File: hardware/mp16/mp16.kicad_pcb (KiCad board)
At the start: 2 copper layers, 76.2 x 104.8 mm, 161 parts, among them J2 OLED SSD1306 I2C, J3 USB-C, J4 MIDI IN, J5 MIDI OUT, J6 EXPANSION, J7 LiPo 1S (pin 1 = GND, pin 2 =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, Q1 DMG2305UX, Q2 MMBT3906, SW1 SHIFT, SW10 P9, SW11 P10, SW12 P11, SW13 P12, SW14 P13, SW15 P14, SW16 P15, SW17 P16, SW18 BOOT, SW19 RESET, SW2 P1, SW20 Power, SW3 P2, SW4 P3, SW5 P4, SW6 P5, SW7 P6, SW8 P7, SW9 P8, U1 74HC165, U10 RP2040, U11 W25Q128JV, U12 USBLC6-2SC6, U13 BQ24074, U15 MAX17048, U16 TPS22917, U17 AP2112K-3.3, U18 MT3608, U19 TLP109, U2 74HC165, U20 USBLC6-2SC6, U3 74HC165, U4 74AHCT1G125, Y1 12MHz

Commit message: BOOT and RESET side by side with labels; fixed-part list; HIDE_REFS
BOOT (SW18) and RESET (SW19) stand side by side in the lower left of the
open bottom shell's window, each named on the bottom silkscreen, the SWD
pads in a row above them (order in hardware/README.md). MIDI In parts
moved to make room. tools/pcb.py: design.HIDE_REFS hides references a
label already names. The side-view charge LED joins the parts that never
move; the battery plug may move (Samuel). Not yet routed.

Co-Authored-By: Claude Opus 5.5 <noreply@anthropic.com>
Claude-Session: https://claude.ai/code/session_01P864NL83Ce2Z2DY4mgeMiF
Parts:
- C55, C56: footprint Capacitor_SMD:C_0402_1005Metric -> Capacitor_SMD:C_0603_1608Metric
- moved SW18 28.5 mm to (68.6, 56.5), turned to -90 degrees
- moved C71 9.28 mm to (57.8, 48.0), turned to -90 degrees
- moved R41 5.69 mm to (57.8, 51.0), turned to -90 degrees
- moved SW19 5.41 mm to (63.4, 56.5), turned to -90 degrees
- moved R11 2.92 mm to (77.5, 53.3)
- moved C54 2.22 mm to (86.4, 59.0)
- moved C56 1.93 mm to (88.5, 59.5), turned to -90 degrees
- moved U19 1.00 mm to (61.0, 49.0)
- moved C55 0.90 mm to (84.4, 59.5), turned to -90 degrees
- moved TP1 0.40 mm to (66.2, 52.6)
- moved TP2 0.40 mm to (68.4, 52.6)
- moved TP3 0.40 mm to (70.6, 52.6)
- moved U16 0.20 mm to (86.6, 56.2)
- moved D22 0.10 mm to (60.8, 43.4)
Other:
- board text added: "BOOT"
- board text added: "PATS MP-16 rev 2"
- board text added: "RESET"

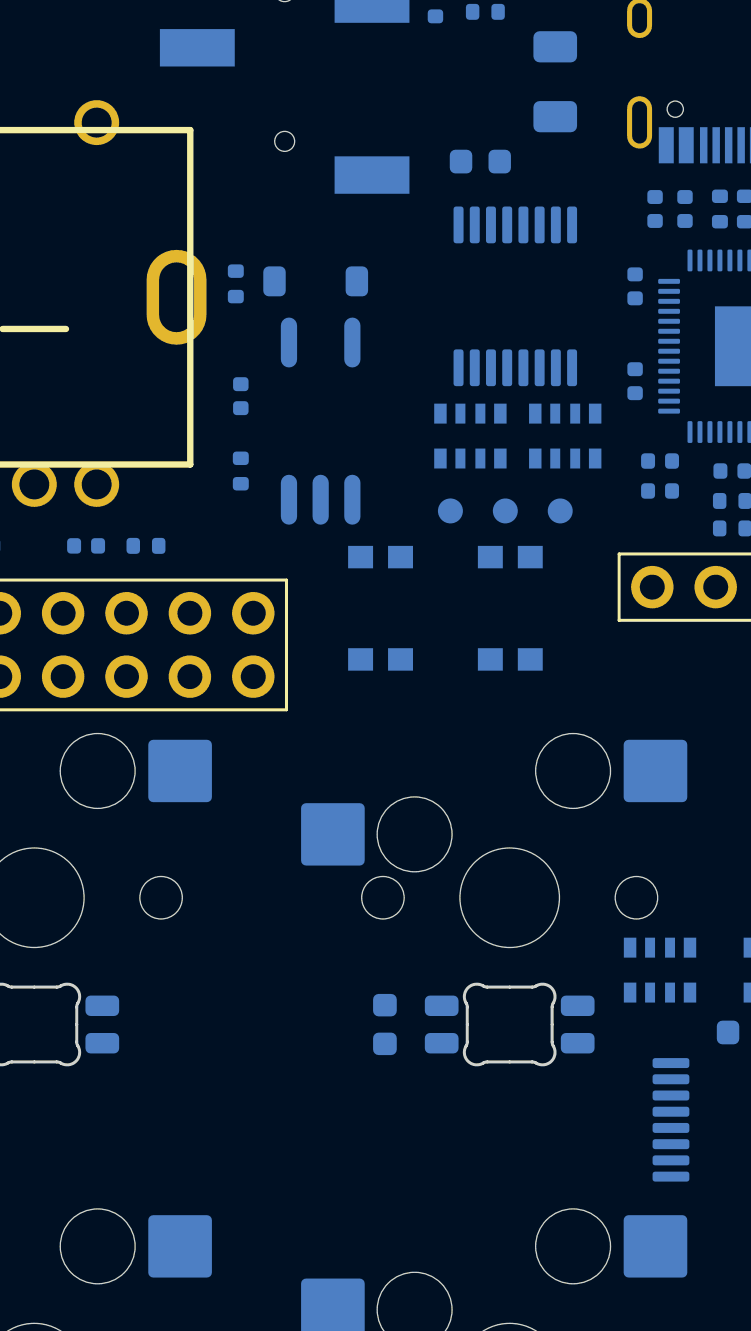
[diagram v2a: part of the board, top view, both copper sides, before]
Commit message: Route 2 result; stitching vias keep hole clearance from bare holes
Route 2 (0.2 mm Supply class): 11 unconnected (was 39) in 9 nets, 7 DRC
errors. Six were stitching vias 0.10-0.23 mm from key-socket holes:
finish.py kept only the drill, not the via's copper, off bare holes.
Placed board with U3 in the key area (route 3 next).

Co-Authored-By: Claude Opus 5.5 <noreply@anthropic.com>
Claude-Session: https://claude.ai/code/session_01P864NL83Ce2Z2DY4mgeMiF
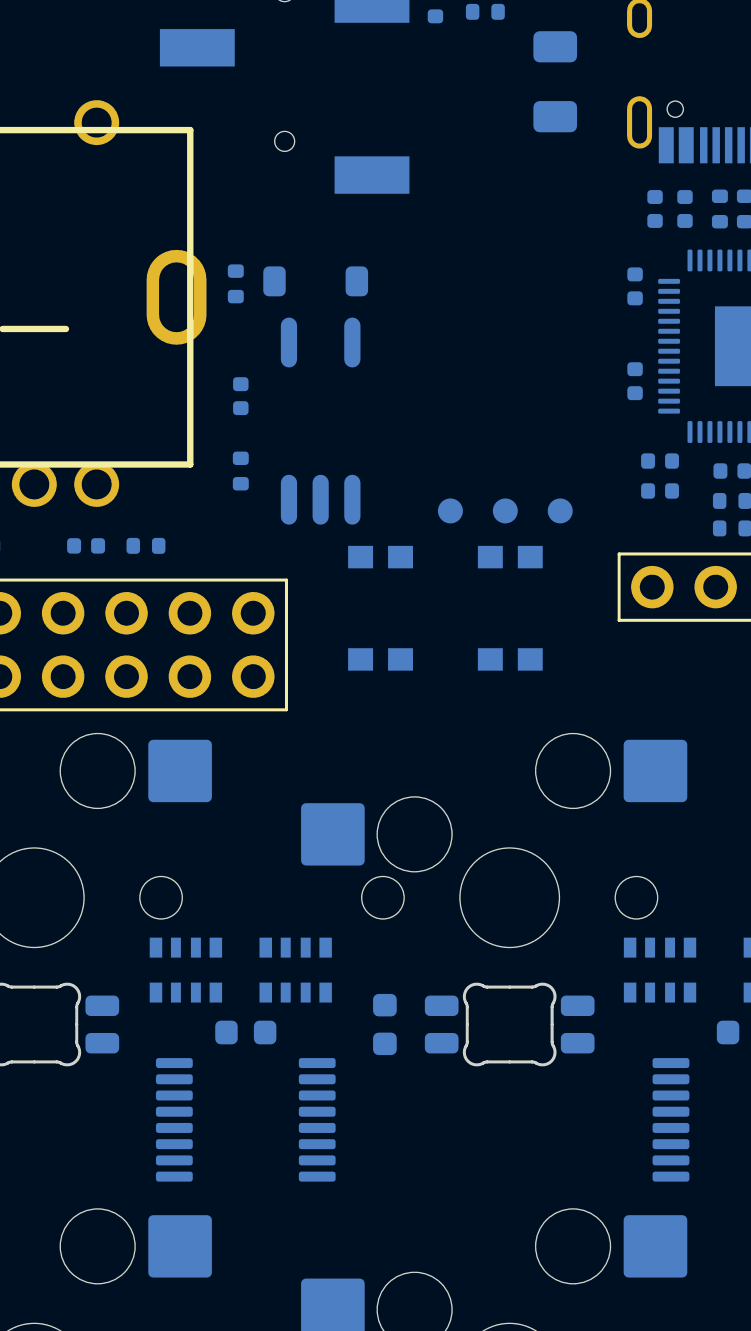
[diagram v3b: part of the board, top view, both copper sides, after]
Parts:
- moved C23 36.1 mm to (58.0, 73.5)
- moved U3 34.7 mm to (58.0, 77.0), turned to 180 degrees
- moved RN5 24.2 mm to (55.6, 71.0)
- moved RN6 24.0 mm to (60.0, 71.0)
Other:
- board text added: "SWD"

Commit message: Route 3 result; RP2040 re-placed with room around it
Route 3 (U3 in the key area): 0 DRC errors, 10 unconnected in 9 nets,
every one at an RP2040 pin (QSPI, VDD_CORE, SWDIO, I2C_SDA, MIDI_RX,
PGOOD_N, EXP_MOSI, AIN1). Its capacitors touched the pin rows and walled
pins in. Now: RP2040 3.8 mm left into the space U3 freed, capacitors
1.9-2.2 mm out opposite their pins (positions computed from the pin
geometry, rp_pin()), a top row for the supply caps and USB/BOOT
resistors, flash against the QSPI corner, crystal under the right half,
and locked escape stubs out of every RP2040 signal pin (ESCAPE).

Co-Authored-By: Claude Opus 5.5 <noreply@anthropic.com>
Claude-Session: https://claude.ai/code/session_01P864NL83Ce2Z2DY4mgeMiF
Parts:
- moved R10 7.72 mm to (78.8, 40.1)
- moved R11 6.07 mm to (71.8, 51.2), turned to -90 degrees
- moved C35 5.11 mm to (74.2, 40.1)
- moved C39 5.11 mm to (75.4, 40.1)
- moved U11 5.08 mm to (84.0, 45.6)
- moved C42 4.90 mm to (82.2, 52.4)
- moved C33 4.37 mm to (69.3, 46.6)
- moved C34 4.34 mm to (69.3, 43.0)
- moved C37 4.21 mm to (71.4, 40.1)
- moved U10 3.82 mm to (74.6, 45.6)
- moved C30 3.16 mm to (79.9, 43.0)
- moved C31 3.16 mm to (79.9, 46.6)
- moved R4 2.24 mm to (85.6, 51.6)
- moved R5 2.24 mm to (86.6, 51.6), turned to 90 degrees
- moved Y1 2.04 mm to (78.6, 51.6)
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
